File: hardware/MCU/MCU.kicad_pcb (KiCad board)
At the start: 2 copper layers, 40 x 40 mm, 41 parts, among them P1 CONN_01X05, P2 CONN_01X04, P3 CONN_01X05, P4 CONN_01X05, U1 MAX6369, U2 TC1262-30VDB, U3 DS18B20, U4 PIC18F45K22, U5 LT6005, Y1 Crystal

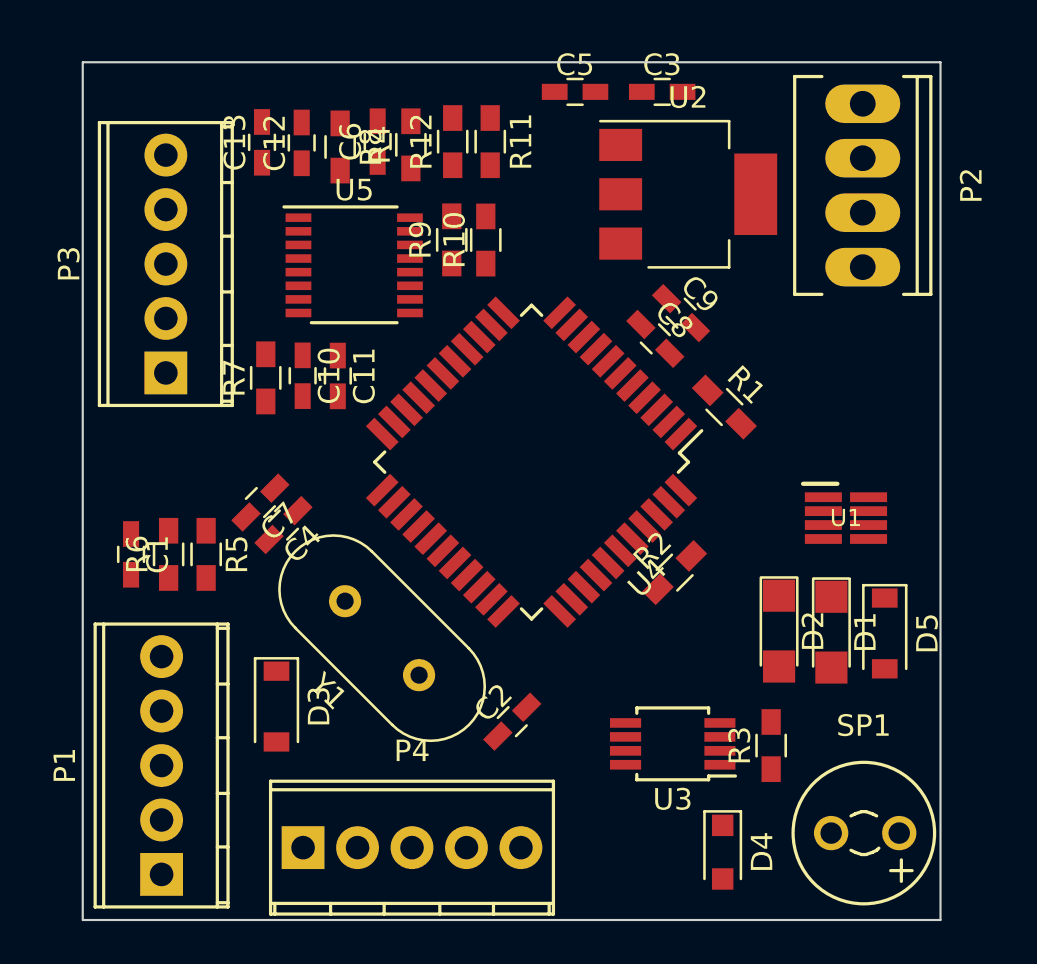
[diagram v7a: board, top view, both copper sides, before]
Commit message: Placa MCU rutada. Falta: - Mejorar la colocación de algunas pistas - Comprobar las reglas para fabricación - Generar los ficheros de fabricación
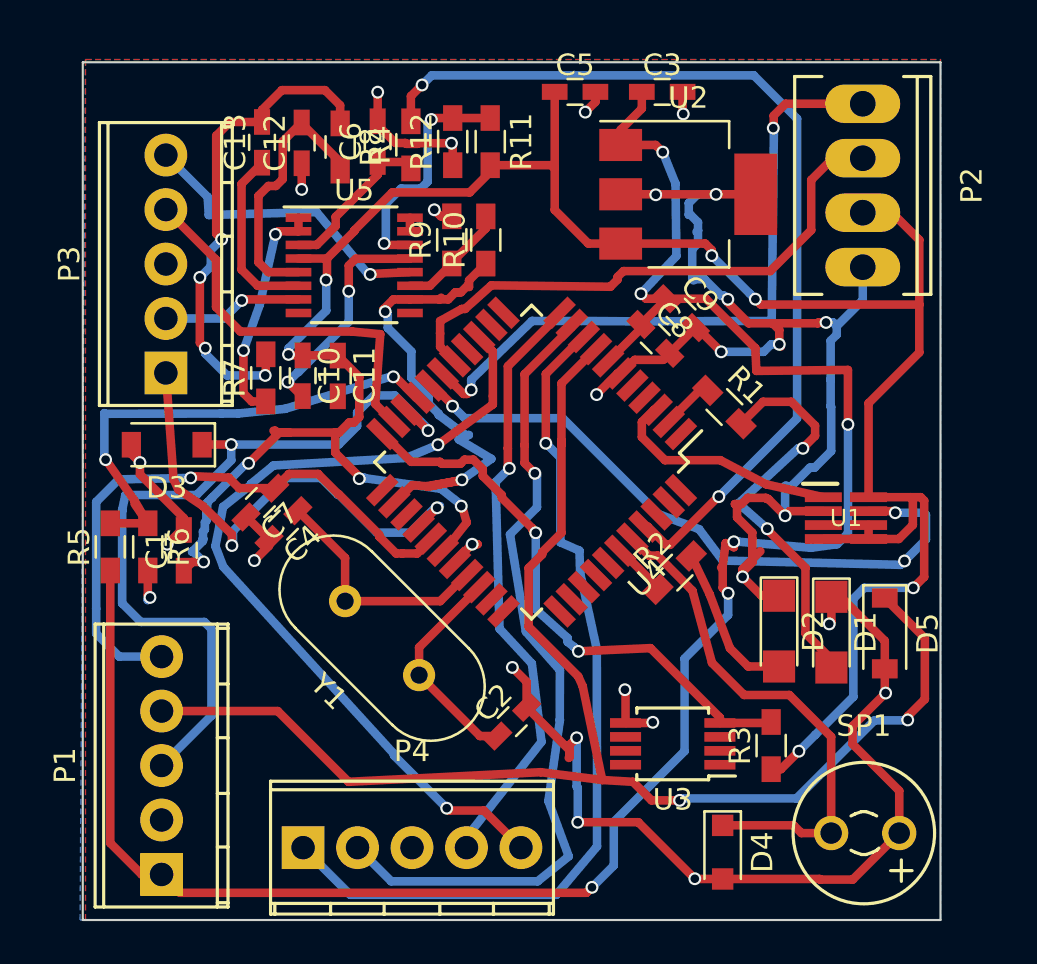
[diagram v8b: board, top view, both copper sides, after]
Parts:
- moved D3 13.2 mm to (16.0, 176.0), turned to 180 degrees
- moved R5 4.48 mm to (13.3, 180.7), turned to 90 degrees
- moved C1 2.47 mm to (16.8, 180.9), turned to 90 degrees
- moved R6 1.03 mm to (15.1, 180.7), turned to 270 degrees
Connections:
- D2 pad 2: (no net) -> Net-(D2-Pad2)
- R2 pad 1: (no net) -> /LED_R
- R2 pad 2: (no net) -> Net-(D2-Pad2)
- U4 pad 39: (no net) -> /LED_R
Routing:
- net GND: track 0.00 -> 135.8 mm, vias 0 -> 30
- net VCC: track 0.00 -> 116.2 mm, vias 0 -> 10
- net VDD: track 0.00 -> 97.1 mm, vias 0 -> 6
- net /PWD: track 0.00 -> 67.6 mm, vias 0 -> 2
- net /BEACON_ON: track 0.00 -> 44.3 mm, vias 0 -> 2
- net /PTT: track 0.00 -> 41.1 mm, vias 0 -> 1
- net /BEACON_MODE: track 0.00 -> 39.9 mm, vias 0 -> 2
- net /RPT: track 0.00 -> 38.2 mm, vias 0 -> 1
- net /SOL: track 0.00 -> 37.5 mm, vias 0 -> 2
- net /PGD: track 0.00 -> 31.4 mm, vias 0 -> 2
- net /~WDO: track 0.00 -> 30.9 mm, vias 0 -> 3
- net /DIS: track 0.00 -> 28.1 mm, vias 0 -> 1
- net /HIPWR: track 0.00 -> 28.1 mm, vias 0 -> 1
- net /TEMP: track 0.00 -> 26.5 mm, vias 0 -> 2
- net /PGC: track 0.00 -> 26.4 mm
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- added copper zone on B.Cu, net GND
- added copper zone on F.Cu, net GND
